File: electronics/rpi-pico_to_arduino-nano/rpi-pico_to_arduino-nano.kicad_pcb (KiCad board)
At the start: 2 copper layers, 41.9 x 52.7 mm, 41 parts, among them U1 Pico

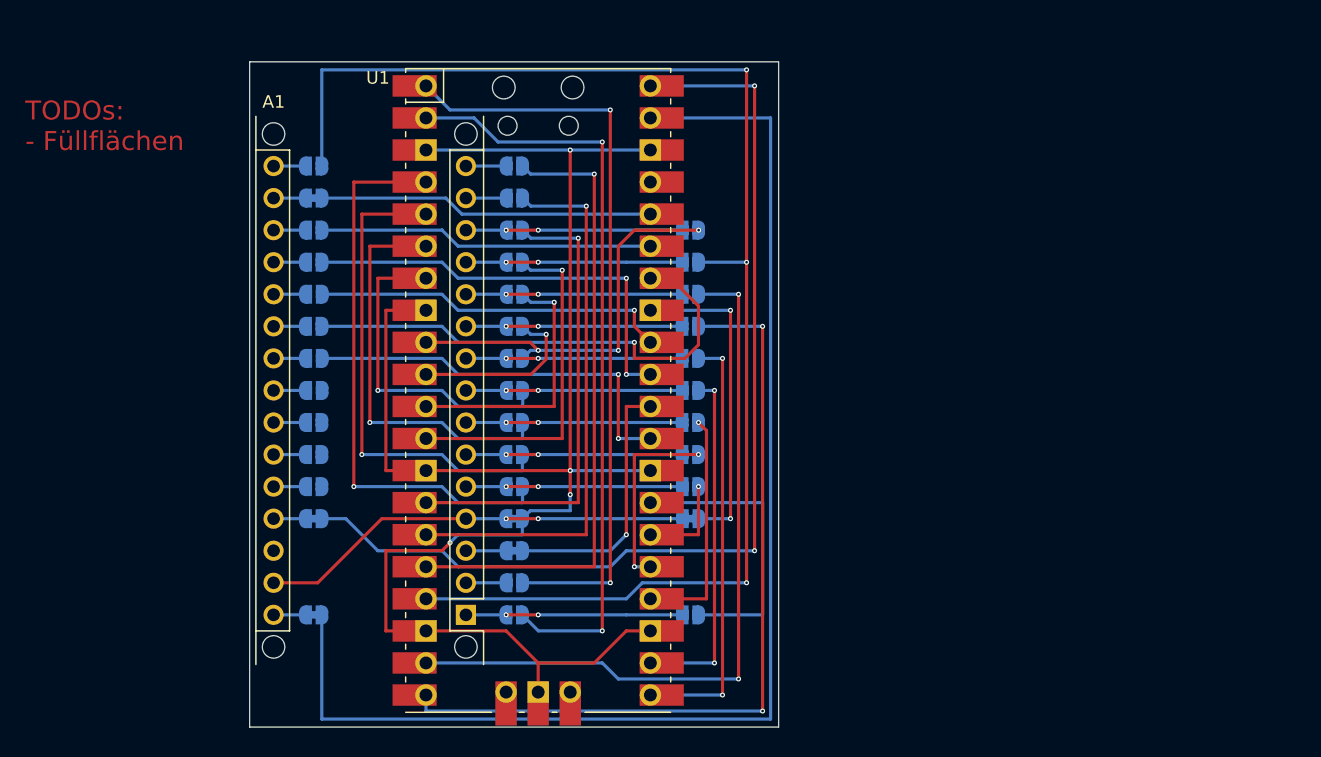
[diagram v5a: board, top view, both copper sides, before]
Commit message: add filled zones
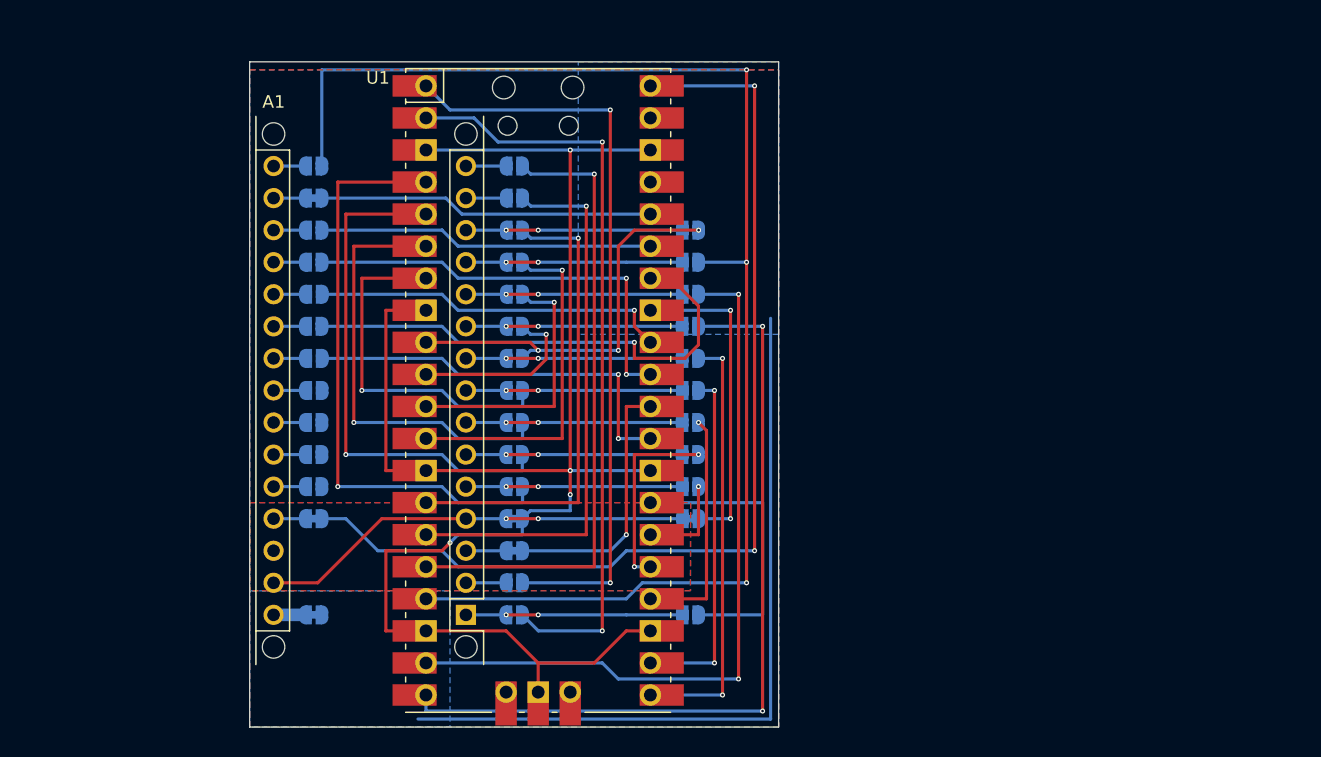
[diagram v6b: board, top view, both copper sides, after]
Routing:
- net /VSYS: track 101.0 -> 59.7 mm
- net /GPIO5: track 25.9 -> 28.5 mm
- net /GPIO4: track 32.3 -> 34.8 mm
- net /GPIO2: track 45.0 -> 47.5 mm
- net /GPIO3: track 38.6 -> 41.2 mm
- added copper zone on B.Cu, net /GND_pico
- added copper zone on F.Cu, net /GND_pico
- added copper zone on B.Cu, net /VSYS
- added copper zone on B.Cu, net GND
- added copper zone on F.Cu, net GND
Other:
- board text removed: "TODOs: - Füllflächen"

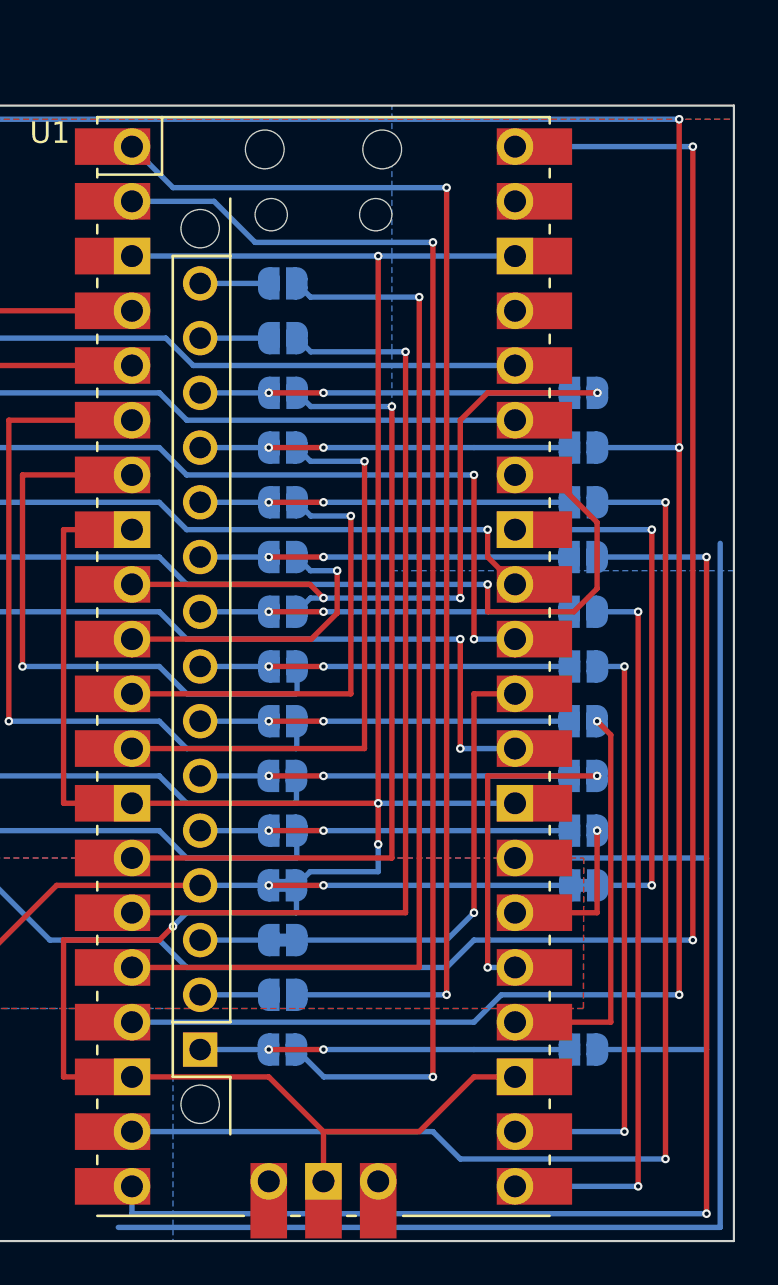
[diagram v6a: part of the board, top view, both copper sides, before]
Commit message: add variables for workflow
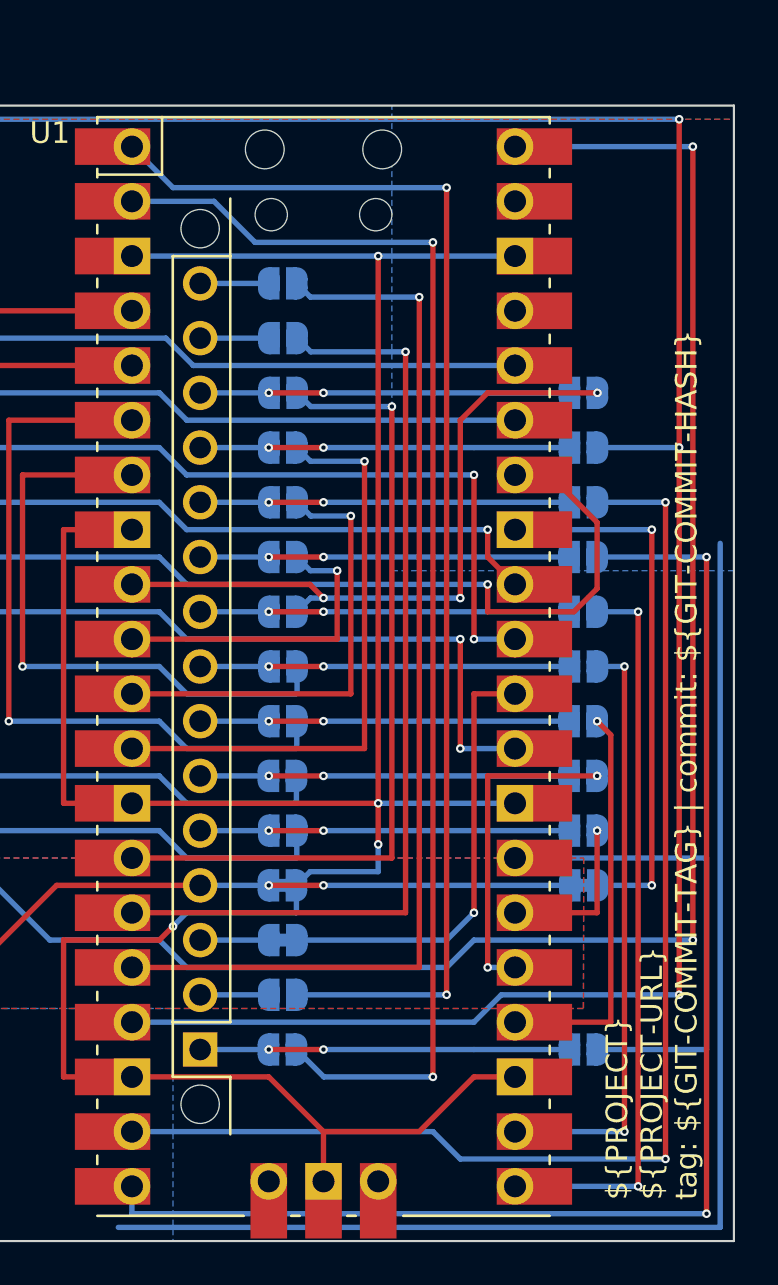
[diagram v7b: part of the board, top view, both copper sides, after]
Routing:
- net /GPIO7: track 14.1 -> 14.8 mm
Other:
- board text added: "${PROJECT} ${PROJECT-URL} tag: ${GIT-COMMIT-TAG} | commit: ${GIT-COMMIT-HASH}"
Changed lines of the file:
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@@
   )
   (paper "A4")
+  (title_block
+    (title "rpi-pico_to_arduino-nano")
+    (comment 1 "${PROJECT}")
+    (comment 2 "${PROJECT-URL}")
+    (comment 3 "${GIT-COMMIT-HASH}")
+    (comment 4 "${GIT-COMMIT-TAG}")
+  )
   (layers
     (0 "F.Cu" signal)
@@
     )
   )
+  (property "GIT-COMMIT-HASH" "noHash")
+  (property "GIT-COMMIT_TAG" "noTag")
+  (property "PROJECT" "BLE-Relay")
+  (property "PROJECT-URL" "https://github.com/erichstuder/BLE-Relay")
   (net 0 "")
   (net 1 "/GPIO1")
@@
   (gr_line (start 130.81 81.28) (end 172.72 81.28) (layer "Edge.Cuts") (width 0.1))
   (gr_line (start 130.81 133.985) (end 130.81 81.28) (layer "Edge.Cuts") (width 0.1))
+  (gr_text "${PROJECT}\n${PROJECT-URL}\ntag: ${GIT-COMMIT-TAG} | commit: ${GIT-COMMIT-HASH}" (at 168.91 132.08 90) (layer "F.SilkS")
+    (effects (font (size 1 1) (thickness 0.15)) (justify left))
+  )
   (segment (start 158.75 87.63) (end 158.75 126.365) (width 0.25) (layer "F.Cu") (net 1))
   (via (at 158.75 126.365) (size 0.4) (drill 0.2) (layers "F.Cu" "B.Cu") (net 1))
@@
   (segment (start 153.67 104.14) (end 160.02 104.14) (width 0.25) (layer "B.Cu") (net 8))
   (segment (start 153.67 104.14) (end 153.065 104.14) (width 0.25) (layer "B.Cu") (net 8))
-  (segment (start 154.305 104.840036) (end 153.100036 106.045) (width 0.25) (layer "F.Cu") (net 9))
-  (segment (start 153.100036 106.045) (end 144.78 106.045) (width 0.25) (layer "F.Cu") (net 9))
-  (segment (start 154.305 102.87) (end 154.305 104.840036) (width 0.25) (layer "F.Cu") (net 9))
+  (segment (start 154.305 102.87) (end 154.305 106.045) (width 0.25) (layer "F.Cu") (net 9))
+  (segment (start 154.305 106.045) (end 144.78 106.045) (width 0.25) (layer "F.Cu") (net 9))
   (via (at 154.305 102.87) (size 0.4) (drill 0.2) (layers "F.Cu" "B.Cu") (net 9))
   (segment (start 154.305 102.87) (end 153.065 102.87) (width 0.25) (layer "B.Cu") (net 9))
